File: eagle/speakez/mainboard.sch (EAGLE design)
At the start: 39 parts, among them U1 +12v

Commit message: added ground rectangle thing
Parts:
- AMBIENT, VOICE: value ADMP621ACEZ-RL7 -> ADMP621ACEZ-RL7-RECT; device InvenSense-INMP621ACEZ-R7:ADMP621ACEZ-RL7 -> InvenSense-INMP621ACEZ-R7-rect:ADMP621ACEZ-RL7-RECT
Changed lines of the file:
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@@
 <?xml version="1.0" encoding="utf-8"?>
 <!DOCTYPE eagle SYSTEM "eagle.dtd">
-<eagle version="7.6.0">
+<eagle version="7.7.0">
 <drawing>
 <settings>
@@
 <part name="SUPPLY1" library="supply2" deviceset="GND" device=""/>
 <part name="SUPPLY2" library="supply2" deviceset="GND" device=""/>
-<part name="AMBIENT" library="InvenSense-INMP621ACEZ-R7" deviceset="ADMP621ACEZ-RL7" device=""/>
-<part name="VOICE" library="InvenSense-INMP621ACEZ-R7" deviceset="ADMP621ACEZ-RL7" device=""/>
+<part name="AMBIENT" library="InvenSense-INMP621ACEZ-R7-rect" deviceset="ADMP621ACEZ-RL7-RECT" device=""/>
+<part name="VOICE" library="InvenSense-INMP621ACEZ-R7-rect" deviceset="ADMP621ACEZ-RL7-RECT" device=""/>
 <part name="TESTPINS" library="pinhead" deviceset="PINHD-1X7" device=""/>
 <part name="SUPPLY8" library="supply2" deviceset="GND" device=""/>

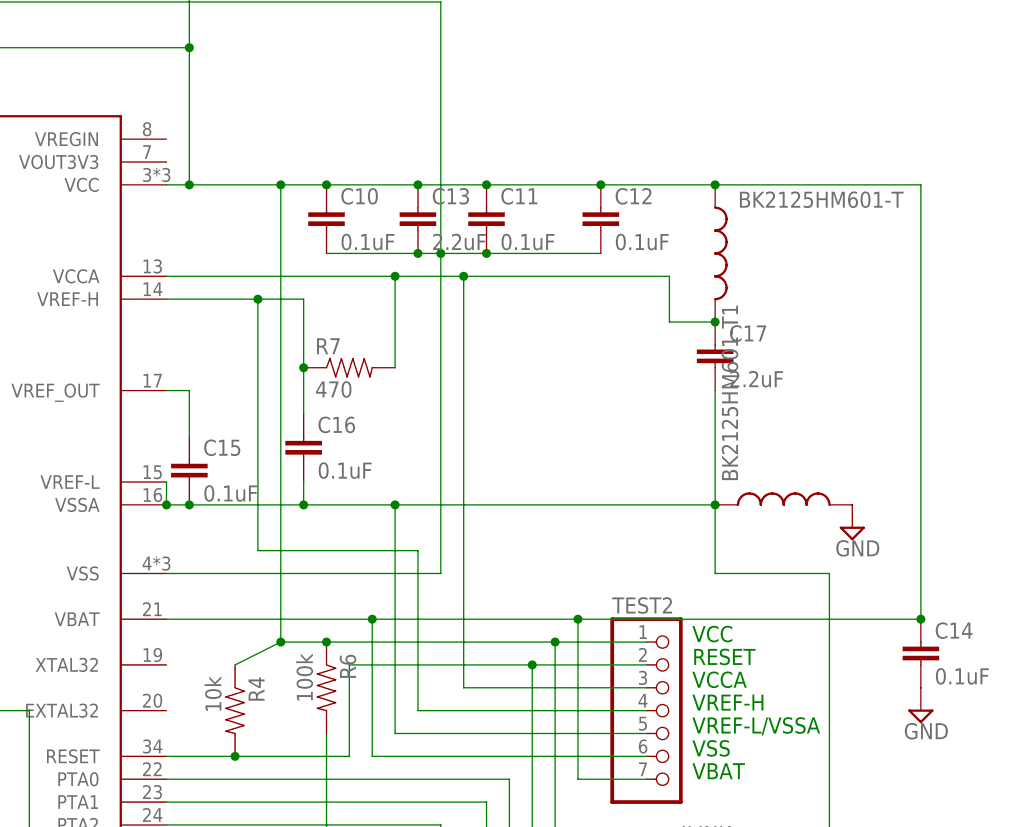
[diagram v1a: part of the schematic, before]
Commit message: added ground plane
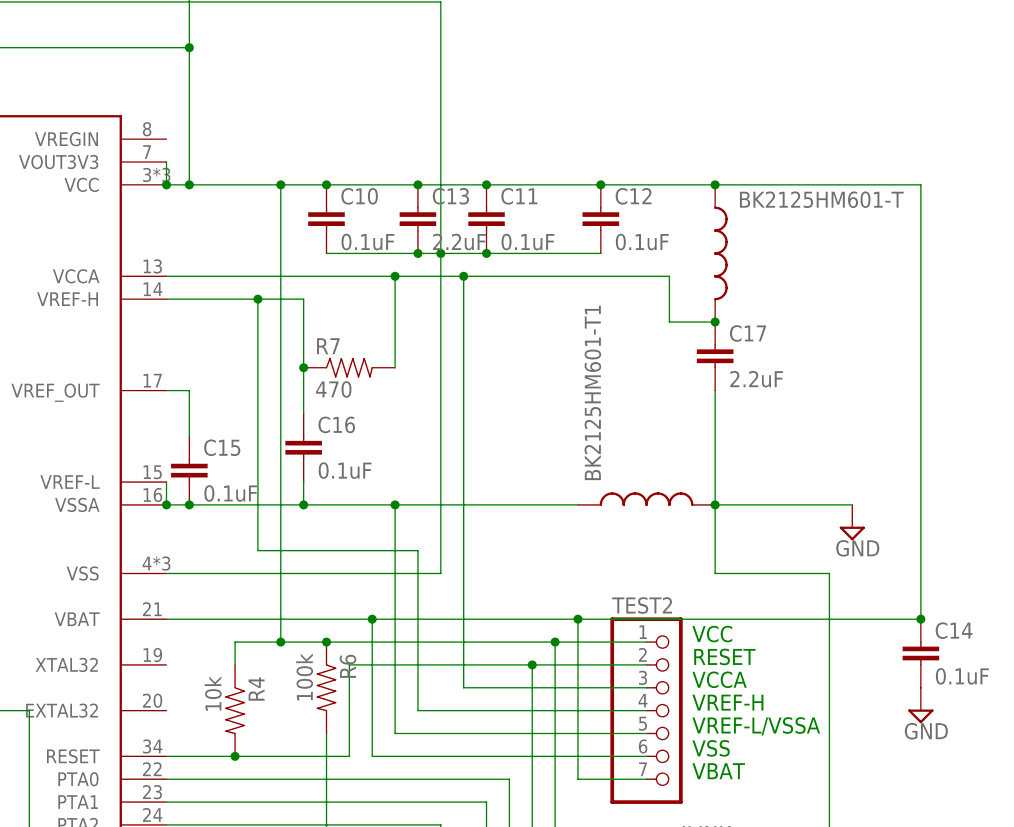
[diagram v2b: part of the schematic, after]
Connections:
- removed net N$29: BK2125HM601-T1.1, C15.2, C16.2, C17.2, JLINK.10, JLINK.12, JLINK.14, JLINK.16, JLINK.18, JLINK.20, JLINK.4, JLINK.6, JLINK.8, TEST2.5, U$1.VREF-L, U$1.VSSA
- removed net N$3: BK2125HM601-T.1, C10.1, C11.1, C12.1, C13.1, C14.1, C4.2, C6.1, C8.1, JLINK.1, R4.1, R6.1, SERIAL.3, TEST2.1, TEST2.6, TEST2.7, U$1.VBAT, U$1.VCC, U1.OUT, VOICE.VDD
- new net DECOUPLED: BK2125HM601-T.1, C10.1, C11.1, C12.1, C13.1, C14.1, C4.2, C6.1, C8.1, JLINK.1, R4.1, R6.1, SERIAL.3, TEST2.1, TEST2.6, TEST2.7, U$1.VBAT, U$1.VCC, U$1.VOUT3V3, U1.OUT, VOICE.VDD
- new net N$20: BK2125HM601-T1.1, C15.2, C16.2, TEST2.5, U$1.VREF-L, U$1.VSSA
- net GND: now also C17.2, JLINK.10, JLINK.12, JLINK.14, JLINK.16, JLINK.18, JLINK.20, JLINK.4, JLINK.6, JLINK.8
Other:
- moved on the sheet: BK2125HM601-T1
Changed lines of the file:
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@@
 <instance part="C16" gate="G$1" x="190.5" y="33.02"/>
 <instance part="C17" gate="G$1" x="236.22" y="43.18"/>
-<instance part="BK2125HM601-T1" gate="G$1" x="243.84" y="27.94" rot="R90"/>
+<instance part="BK2125HM601-T1" gate="G$1" x="228.6" y="27.94" rot="R90"/>
 <instance part="SUPPLY9" gate="GND" x="251.46" y="25.4"/>
 <instance part="JLINK" gate="A" x="238.76" y="-22.86"/>
@@
 <pinref part="BK2125HM601-T1" gate="G$1" pin="2"/>
 <pinref part="SUPPLY9" gate="GND" pin="GND"/>
+<wire x1="236.22" y1="27.94" x2="251.46" y2="27.94" width="0.1524" layer="91"/>
+<pinref part="C17" gate="G$1" pin="2"/>
+<wire x1="236.22" y1="40.64" x2="236.22" y2="27.94" width="0.1524" layer="91"/>
+<junction x="236.22" y="27.94"/>
+<wire x1="236.22" y1="20.32" x2="248.92" y2="20.32" width="0.1524" layer="91"/>
+<pinref part="JLINK" gate="A" pin="4"/>
+<wire x1="243.84" y1="-15.24" x2="248.92" y2="-15.24" width="0.1524" layer="91"/>
+<wire x1="248.92" y1="-15.24" x2="248.92" y2="-17.78" width="0.1524" layer="91"/>
+<pinref part="JLINK" gate="A" pin="6"/>
+<wire x1="248.92" y1="-17.78" x2="243.84" y2="-17.78" width="0.1524" layer="91"/>
+<wire x1="248.92" y1="-17.78" x2="248.92" y2="-20.32" width="0.1524" layer="91"/>
+<junction x="248.92" y="-17.78"/>
+<pinref part="JLINK" gate="A" pin="8"/>
+<wire x1="248.92" y1="-20.32" x2="243.84" y2="-20.32" width="0.1524" layer="91"/>
+<wire x1="248.92" y1="-20.32" x2="248.92" y2="-22.86" width="0.1524" layer="91"/>
+<junction x="248.92" y="-20.32"/>
+<pinref part="JLINK" gate="A" pin="10"/>
+<wire x1="248.92" y1="-22.86" x2="243.84" y2="-22.86" width="0.1524" layer="91"/>
+<wire x1="248.92" y1="-22.86" x2="248.92" y2="-25.4" width="0.1524" layer="91"/>
+<junction x="248.92" y="-22.86"/>
+<pinref part="JLINK" gate="A" pin="12"/>
+<wire x1="248.92" y1="-25.4" x2="243.84" y2="-25.4" width="0.1524" layer="91"/>
+<wire x1="248.92" y1="-25.4" x2="248.92" y2="-27.94" width="0.1524" layer="91"/>
+<junction x="248.92" y="-25.4"/>
+<pinref part="JLINK" gate="A" pin="14"/>
+<wire x1="248.92" y1="-27.94" x2="243.84" y2="-27.94" width="0.1524" layer="91"/>
+<wire x1="248.92" y1="-27.94" x2="248.92" y2="-30.48" width="0.1524" layer="91"/>
+<junction x="248.92" y="-27.94"/>
+<pinref part="JLINK" gate="A" pin="16"/>
+<wire x1="248.92" y1="-30.48" x2="243.84" y2="-30.48" width="0.1524" layer="91"/>
+<wire x1="248.92" y1="-30.48" x2="248.92" y2="-33.02" width="0.1524" layer="91"/>
+<junction x="248.92" y="-30.48"/>
+<pinref part="JLINK" gate="A" pin="18"/>
+<wire x1="248.92" y1="-33.02" x2="243.84" y2="-33.02" width="0.1524" layer="91"/>
+<wire x1="248.92" y1="-33.02" x2="248.92" y2="-35.56" width="0.1524" layer="91"/>
+<junction x="248.92" y="-33.02"/>
+<pinref part="JLINK" gate="A" pin="20"/>
+<wire x1="248.92" y1="-35.56" x2="243.84" y2="-35.56" width="0.1524" layer="91"/>
+<wire x1="248.92" y1="20.32" x2="248.92" y2="-15.24" width="0.1524" layer="91"/>
+<junction x="248.92" y="-15.24"/>
+<wire x1="236.22" y1="27.94" x2="236.22" y2="20.32" width="0.1524" layer="91"/>
 </segment>
 </net>
@@
 </segment>
 </net>
-<net name="N$3" class="0">
+<net name="DECOUPLED" class="0">
 <segment>
 <pinref part="U$1" gate="G$1" pin="VBAT"/>
@@
 <pinref part="JLINK" gate="A" pin="1"/>
 <wire x1="218.44" y1="-12.7" x2="236.22" y2="-12.7" width="0.1524" layer="91"/>
-<pinref part="R4" gate="G$1" pin="1"/>
-<wire x1="182.88" y1="10.16" x2="187.96" y2="12.7" width="0.1524" layer="91"/>
-<junction x="187.96" y="12.7"/>
 <pinref part="R6" gate="G$1" pin="1"/>
 <junction x="193.04" y="12.7"/>
+<pinref part="U$1" gate="G$1" pin="VOUT3V3"/>
+<wire x1="175.26" y1="66.04" x2="175.26" y2="63.5" width="0.1524" layer="91"/>
+<junction x="175.26" y="63.5"/>
+<wire x1="187.96" y1="12.7" x2="182.88" y2="12.7" width="0.1524" layer="91"/>
+<junction x="187.96" y="12.7"/>
+<pinref part="R4" gate="G$1" pin="1"/>
+<wire x1="182.88" y1="12.7" x2="182.88" y2="10.16" width="0.1524" layer="91"/>
 </segment>
 </net>
@@
 <wire x1="-12.7" y1="35.56" x2="-15.24" y2="35.56" width="0.1524" layer="91"/>
 <wire x1="-15.24" y1="35.56" x2="-15.24" y2="-30.48" width="0.1524" layer="91"/>
-</segment>
-</net>
-<net name="N$29" class="0">
-<segment>
-<pinref part="U$1" gate="G$1" pin="VREF-L"/>
-<pinref part="U$1" gate="G$1" pin="VSSA"/>
-<wire x1="175.26" y1="30.48" x2="175.26" y2="27.94" width="0.1524" layer="91"/>
-<pinref part="C15" gate="G$1" pin="2"/>
-<wire x1="175.26" y1="27.94" x2="177.8" y2="27.94" width="0.1524" layer="91"/>
-<junction x="175.26" y="27.94"/>
-<pinref part="C17" gate="G$1" pin="2"/>
-<wire x1="177.8" y1="27.94" x2="190.5" y2="27.94" width="0.1524" layer="91"/>
-<wire x1="190.5" y1="27.94" x2="200.66" y2="27.94" width="0.1524" layer="91"/>
-<wire x1="200.66" y1="27.94" x2="236.22" y2="27.94" width="0.1524" layer="91"/>
-<wire x1="236.22" y1="27.94" x2="236.22" y2="40.64" width="0.1524" layer="91"/>
-<junction x="177.8" y="27.94"/>
-<pinref part="C16" gate="G$1" pin="2"/>
-<wire x1="190.5" y1="30.48" x2="190.5" y2="27.94" width="0.1524" layer="91"/>
-<junction x="190.5" y="27.94"/>
-<pinref part="BK2125HM601-T1" gate="G$1" pin="1"/>
-<junction x="236.22" y="27.94"/>
-<wire x1="200.66" y1="27.94" x2="200.66" y2="2.54" width="0.1524" layer="91"/>
-<junction x="200.66" y="27.94"/>
-<pinref part="TEST2" gate="A" pin="5"/>
-<wire x1="200.66" y1="2.54" x2="228.6" y2="2.54" width="0.1524" layer="91"/>
-<wire x1="236.22" y1="27.94" x2="236.22" y2="20.32" width="0.1524" layer="91"/>
-<wire x1="236.22" y1="20.32" x2="248.92" y2="20.32" width="0.1524" layer="91"/>
-<pinref part="JLINK" gate="A" pin="4"/>
-<wire x1="243.84" y1="-15.24" x2="248.92" y2="-15.24" width="0.1524" layer="91"/>
-<wire x1="248.92" y1="-15.24" x2="248.92" y2="-17.78" width="0.1524" layer="91"/>
-<pinref part="JLINK" gate="A" pin="6"/>
-<wire x1="248.92" y1="-17.78" x2="243.84" y2="-17.78" width="0.1524" layer="91"/>
-<wire x1="248.92" y1="-17.78" x2="248.92" y2="-20.32" width="0.1524" layer="91"/>
-<junction x="248.92" y="-17.78"/>
-<pinref part="JLINK" gate="A" pin="8"/>
-<wire x1="248.92" y1="-20.32" x2="243.84" y2="-20.32" width="0.1524" layer="91"/>
-<wire x1="248.92" y1="-20.32" x2="248.92" y2="-22.86" width="0.1524" layer="91"/>
-<junction x="248.92" y="-20.32"/>
-<pinref part="JLINK" gate="A" pin="10"/>
-<wire x1="248.92" y1="-22.86" x2="243.84" y2="-22.86" width="0.1524" layer="91"/>
-<wire x1="248.92" y1="-22.86" x2="248.92" y2="-25.4" width="0.1524" layer="91"/>
-<junction x="248.92" y="-22.86"/>
-<pinref part="JLINK" gate="A" pin="12"/>
-<wire x1="248.92" y1="-25.4" x2="243.84" y2="-25.4" width="0.1524" layer="91"/>
-<wire x1="248.92" y1="-25.4" x2="248.92" y2="-27.94" width="0.1524" layer="91"/>
-<junction x="248.92" y="-25.4"/>
-<pinref part="JLINK" gate="A" pin="14"/>
-<wire x1="248.92" y1="-27.94" x2="243.84" y2="-27.94" width="0.1524" layer="91"/>
-<wire x1="248.92" y1="-27.94" x2="248.92" y2="-30.48" width="0.1524" layer="91"/>
-<junction x="248.92" y="-27.94"/>
-<pinref part="JLINK" gate="A" pin="16"/>
-<wire x1="248.92" y1="-30.48" x2="243.84" y2="-30.48" width="0.1524" layer="91"/>
-<wire x1="248.92" y1="-30.48" x2="248.92" y2="-33.02" width="0.1524" layer="91"/>
-<junction x="248.92" y="-30.48"/>
-<pinref part="JLINK" gate="A" pin="18"/>
-<wire x1="248.92" y1="-33.02" x2="243.84" y2="-33.02" width="0.1524" layer="91"/>
-<wire x1="248.92" y1="-33.02" x2="248.92" y2="-35.56" width="0.1524" layer="91"/>
-<junction x="248.92" y="-33.02"/>
-<pinref part="JLINK" gate="A" pin="20"/>
-<wire x1="248.92" y1="-35.56" x2="243.84" y2="-35.56" width="0.1524" layer="91"/>
-<wire x1="248.92" y1="20.32" x2="248.92" y2="-15.24" width="0.1524" layer="91"/>
-<junction x="248.92" y="-15.24"/>
 </segment>
 </net>
@@
 </segment>
 </net>
+<net name="N$20" class="0">
+<segment>
+<pinref part="TEST2" gate="A" pin="5"/>
+<pinref part="C15" gate="G$1" pin="2"/>
+<pinref part="U$1" gate="G$1" pin="VSSA"/>
+<pinref part="U$1" gate="G$1" pin="VREF-L"/>
+<wire x1="175.26" y1="30.48" x2="175.26" y2="27.94" width="0.1524" layer="91"/>
+<junction x="175.26" y="27.94"/>
+<wire x1="175.26" y1="27.94" x2="177.8" y2="27.94" width="0.1524" layer="91"/>
+<junction x="177.8" y="27.94"/>
+<wire x1="177.8" y1="27.94" x2="190.5" y2="27.94" width="0.1524" layer="91"/>
+<pinref part="C16" gate="G$1" pin="2"/>
+<wire x1="190.5" y1="30.48" x2="190.5" y2="27.94" width="0.1524" layer="91"/>
+<junction x="190.5" y="27.94"/>
+<wire x1="190.5" y1="27.94" x2="200.66" y2="27.94" width="0.1524" layer="91"/>
+<wire x1="200.66" y1="27.94" x2="200.66" y2="2.54" width="0.1524" layer="91"/>
+<wire x1="200.66" y1="2.54" x2="228.6" y2="2.54" width="0.1524" layer="91"/>
+<pinref part="BK2125HM601-T1" gate="G$1" pin="1"/>
+<wire x1="220.98" y1="27.94" x2="200.66" y2="27.94" width="0.1524" layer="91"/>
+<junction x="200.66" y="27.94"/>
+</segment>
+</net>

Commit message: routed some of board
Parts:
- C1, C2: device rcl:C-USC0805 -> SparkFun-Capacitors:CAP0805
- R1, R2: device rcl:R-US_M0805 -> SparkFun-Passives:RESISTOR0805-RES
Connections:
- net N$4 renamed DATA
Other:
- moved on the sheet: C1, C2
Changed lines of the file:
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@@
 </classes>
 <parts>
-<part name="R1" library="rcl" deviceset="R-US_" device="M0805" value="5kohm"/>
-<part name="R2" library="rcl" deviceset="R-US_" device="M0805" value="5kohm"/>
-<part name="C1" library="rcl" deviceset="C-US" device="C0805" value="100pf"/>
-<part name="C2" library="rcl" deviceset="C-US" device="C0805" value="100pf"/>
+<part name="R1" library="SparkFun-Passives" deviceset="RESISTOR" device="0805-RES" value="5kohm"/>
+<part name="R2" library="SparkFun-Passives" deviceset="RESISTOR" device="0805-RES" value="5kohm"/>
+<part name="C1" library="SparkFun-Capacitors" deviceset="CAP" device="0805" value="100pf"/>
+<part name="C2" library="SparkFun-Capacitors" deviceset="CAP" device="0805" value="100pf"/>
 <part name="SUPPLY1" library="supply2" deviceset="GND" device=""/>
 <part name="SUPPLY2" library="supply2" deviceset="GND" device=""/>
@@
 <pinref part="R1" gate="G$1" pin="2"/>
 <pinref part="C1" gate="G$1" pin="1"/>
-<wire x1="58.42" y1="60.96" x2="83.82" y2="60.96" width="0.1524" layer="91"/>
-<junction x="58.42" y="60.96"/>
+<wire x1="58.42" y1="63.5" x2="83.82" y2="60.96" width="0.1524" layer="91"/>
+<junction x="58.42" y="63.5"/>
 <wire x1="83.82" y1="60.96" x2="83.82" y2="38.1" width="0.1524" layer="91"/>
 <wire x1="83.82" y1="38.1" x2="83.82" y2="2.54" width="0.1524" layer="91"/>
@@
 <pinref part="TESTPINS" gate="A" pin="4"/>
 <wire x1="-22.86" y1="43.18" x2="-12.7" y2="43.18" width="0.1524" layer="91"/>
+<wire x1="58.42" y1="60.96" x2="58.42" y2="63.5" width="0.1524" layer="91"/>
 </segment>
 </net>
@@
 <pinref part="R2" gate="G$1" pin="2"/>
 <pinref part="C2" gate="G$1" pin="1"/>
-<wire x1="58.42" y1="30.48" x2="58.42" y2="27.94" width="0.1524" layer="91"/>
 <wire x1="58.42" y1="30.48" x2="66.04" y2="30.48" width="0.1524" layer="91"/>
 <wire x1="66.04" y1="30.48" x2="66.04" y2="5.08" width="0.1524" layer="91"/>
@@
 <pinref part="C1" gate="G$1" pin="2"/>
 <pinref part="SUPPLY1" gate="GND" pin="GND"/>
+<wire x1="58.42" y1="53.34" x2="58.42" y2="55.88" width="0.1524" layer="91"/>
 </segment>
 <segment>
 <pinref part="C2" gate="G$1" pin="2"/>
 <pinref part="SUPPLY2" gate="GND" pin="GND"/>
+<wire x1="58.42" y1="20.32" x2="58.42" y2="22.86" width="0.1524" layer="91"/>
 </segment>
 <segment>
@@
 </segment>
 </net>
-<net name="N$4" class="0">
+<net name="DATA" class="0">
 <segment>
 <pinref part="VOICE" gate="A" pin="DATA"/>

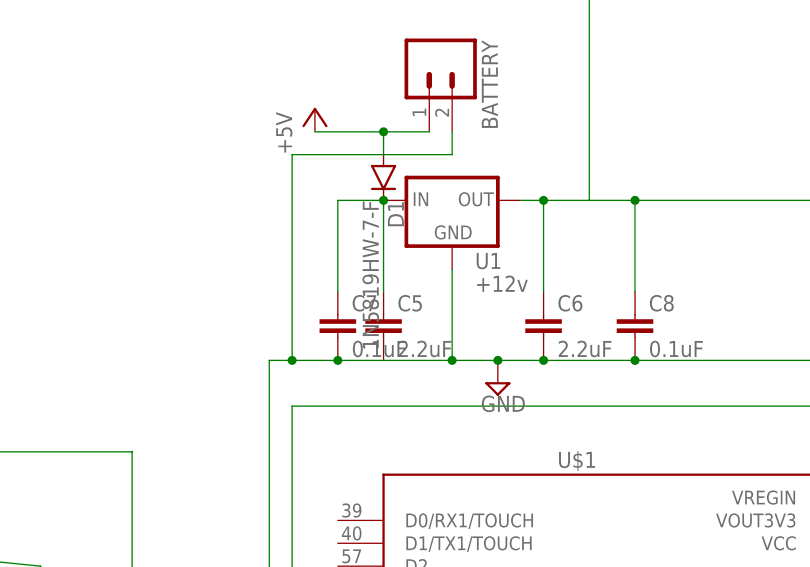
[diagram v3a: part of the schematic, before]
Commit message: finished routing board
Didn't check for overlaps yet. Need to fix mic library.
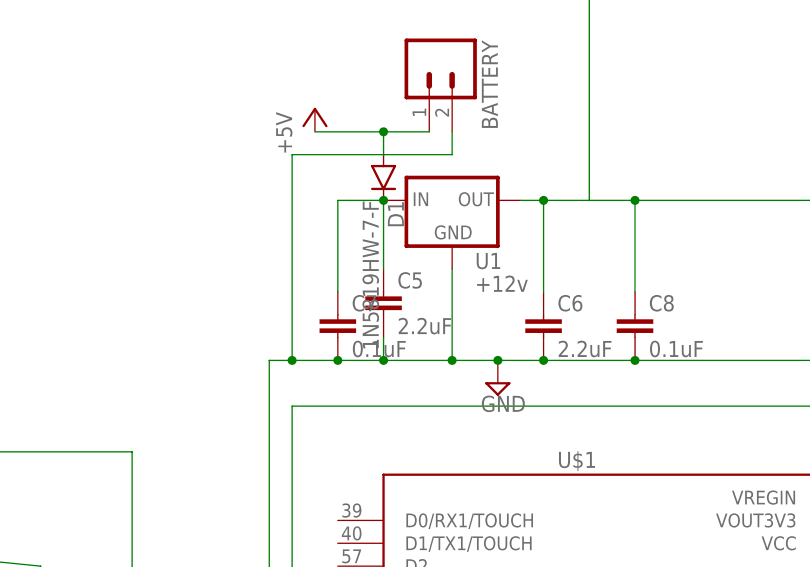
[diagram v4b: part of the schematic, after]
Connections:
- net GND: now also C5.2
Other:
- moved on the sheet: C5
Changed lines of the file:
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@@
 <instance part="U$1" gate="G$1" x="144.78" y="15.24"/>
 <instance part="U1" gate="G$1" x="129.54" y="101.6"/>
-<instance part="C5" gate="G$1" x="121.92" y="86.36"/>
+<instance part="C5" gate="G$1" x="121.92" y="88.9"/>
 <instance part="C6" gate="G$1" x="139.7" y="86.36"/>
 <instance part="C7" gate="G$1" x="116.84" y="86.36"/>
@@
 <wire x1="111.76" y1="83.82" x2="116.84" y2="83.82" width="0.1524" layer="91"/>
 <pinref part="U1" gate="G$1" pin="GND"/>
-<wire x1="116.84" y1="83.82" x2="129.54" y2="83.82" width="0.1524" layer="91"/>
+<wire x1="116.84" y1="83.82" x2="121.92" y2="83.82" width="0.1524" layer="91"/>
+<wire x1="121.92" y1="83.82" x2="129.54" y2="83.82" width="0.1524" layer="91"/>
 <wire x1="129.54" y1="83.82" x2="129.54" y2="93.98" width="0.1524" layer="91"/>
 <pinref part="C6" gate="G$1" pin="2"/>
@@
 <pinref part="SUPPLY7" gate="GND" pin="GND"/>
 <junction x="134.62" y="83.82"/>
+<wire x1="121.92" y1="83.82" x2="121.92" y2="86.36" width="0.1524" layer="91"/>
+<junction x="121.92" y="83.82"/>
+<pinref part="C5" gate="G$1" pin="2"/>
 </segment>
 <segment>
@@
 <pinref part="D1" gate="G$1" pin="C"/>
 <pinref part="C5" gate="G$1" pin="1"/>
-<wire x1="121.92" y1="101.6" x2="121.92" y2="91.44" width="0.1524" layer="91"/>
+<wire x1="121.92" y1="101.6" x2="121.92" y2="93.98" width="0.1524" layer="91"/>
 <junction x="121.92" y="101.6"/>
 <wire x1="121.92" y1="101.6" x2="116.84" y2="101.6" width="0.1524" layer="91"/>
